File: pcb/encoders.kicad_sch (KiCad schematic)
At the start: 10 parts, among them J1 GPIO, J2 Screw_Terminal_01x04, J3 Screw_Terminal_01x04, J4 Screw_Terminal_01x04

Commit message: update PCB to add two more terminals
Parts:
- added J5, J6: Screw_Terminal_01x04, TerminalBlock_Phoenix:TerminalBlock_Phoenix_PT-1,5-4-5.0-H_1x04_P5.00mm_Horizontal, symbol Connector:Screw_Terminal_01x04
- added R10, R7, R8, R9: 4.7K, Resistor_THT:R_Axial_DIN0207_L6.3mm_D2.5mm_P7.62mm_Horizontal, symbol Device:R
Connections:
- net +3V3: now also R10.1, R7.1, R8.1, R9.1; no longer J1.17 (Pin_17)
- net +5V: now also J5.4 (Pin_4), J6.4 (Pin_4)
- net GND: now also J5.1 (Pin_1), J6.1 (Pin_1)
- net GPIO10/SPI0.MOSI: now also J5.3 (Pin_3), R7.2
- net GPIO11/SPI0.SCLK: now also J6.3 (Pin_3), R9.2
- net GPIO17: now also R4.2; no longer R3.2
- net GPIO22: now also J4.2 (Pin_2), R6.2
- net GPIO27: now also J4.3 (Pin_3), R5.2; no longer J3.3 (Pin_3), R4.2
- net GPIO2/SDA1: now also J2.3 (Pin_3); no longer J2.2 (Pin_2)
- net GPIO3/SCL1: now also J2.2 (Pin_2); no longer J2.3 (Pin_3)
- net GPIO4/GPCLK0: now also J3.3 (Pin_3), R3.2
- net GPIO5: now also J6.2 (Pin_2), R10.2; no longer J4.2 (Pin_2), R5.2
- net GPIO6: no longer J4.3 (Pin_3), R6.2
- net GPIO9/SPI0.MISO: now also J5.2 (Pin_2), R8.2
- no-connect marks 22 -> 19
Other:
- moved on the sheet: J1, J2, J3, J4, R1, R2, R3, R4, R5, R6

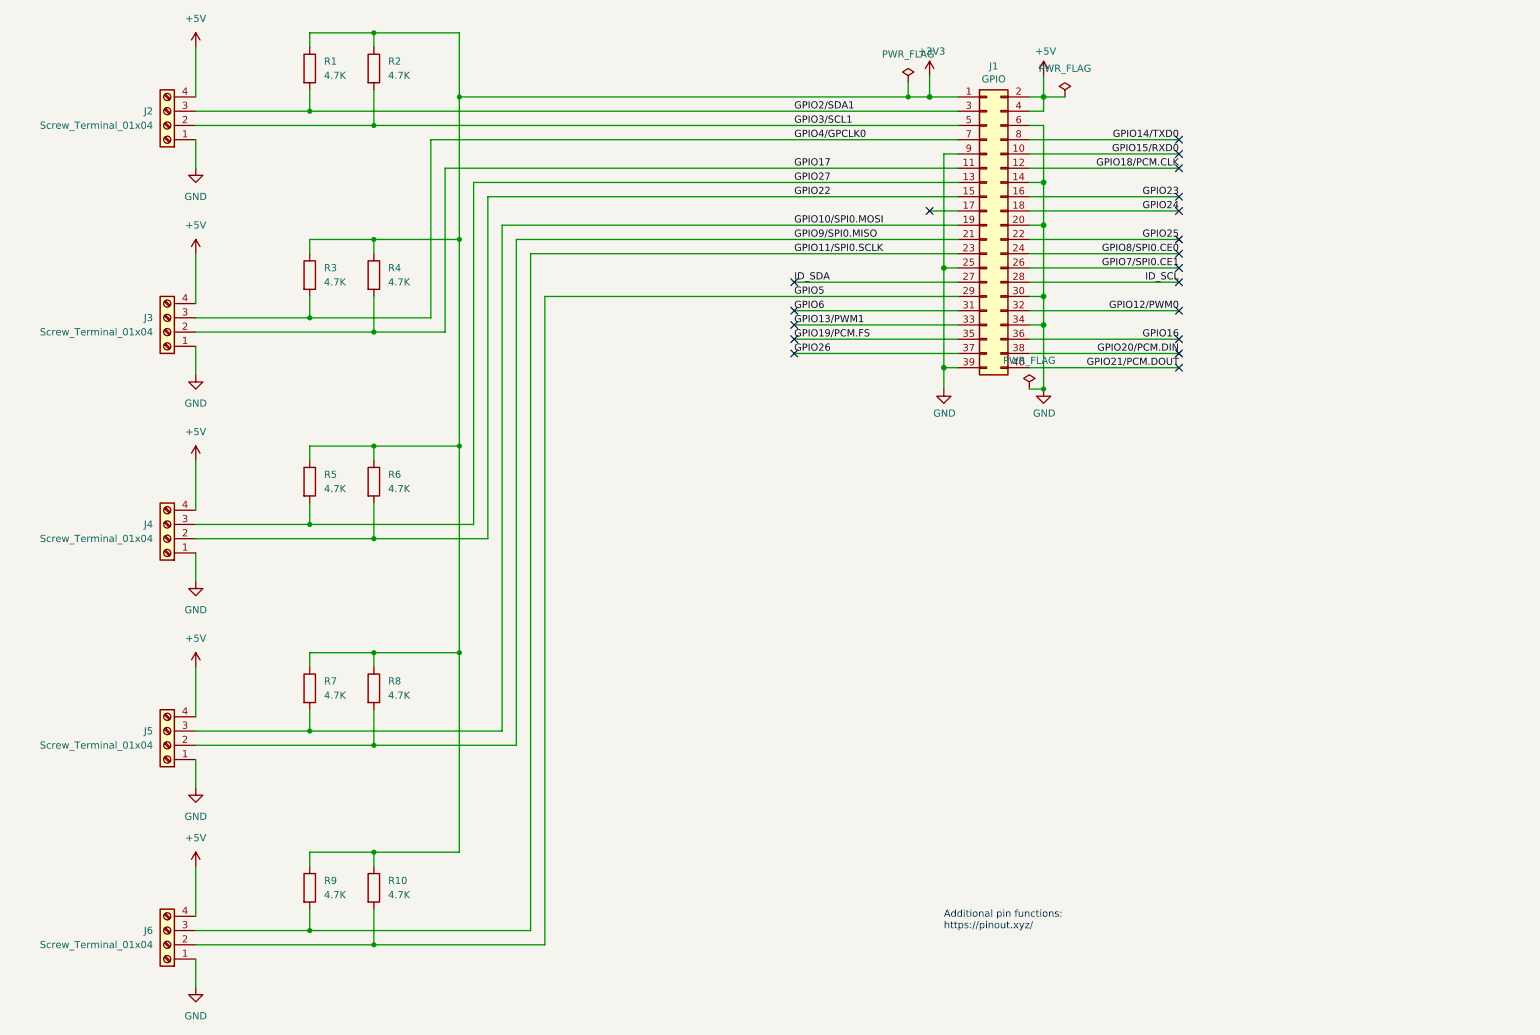
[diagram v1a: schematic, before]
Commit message: updated schematic using ls7466s
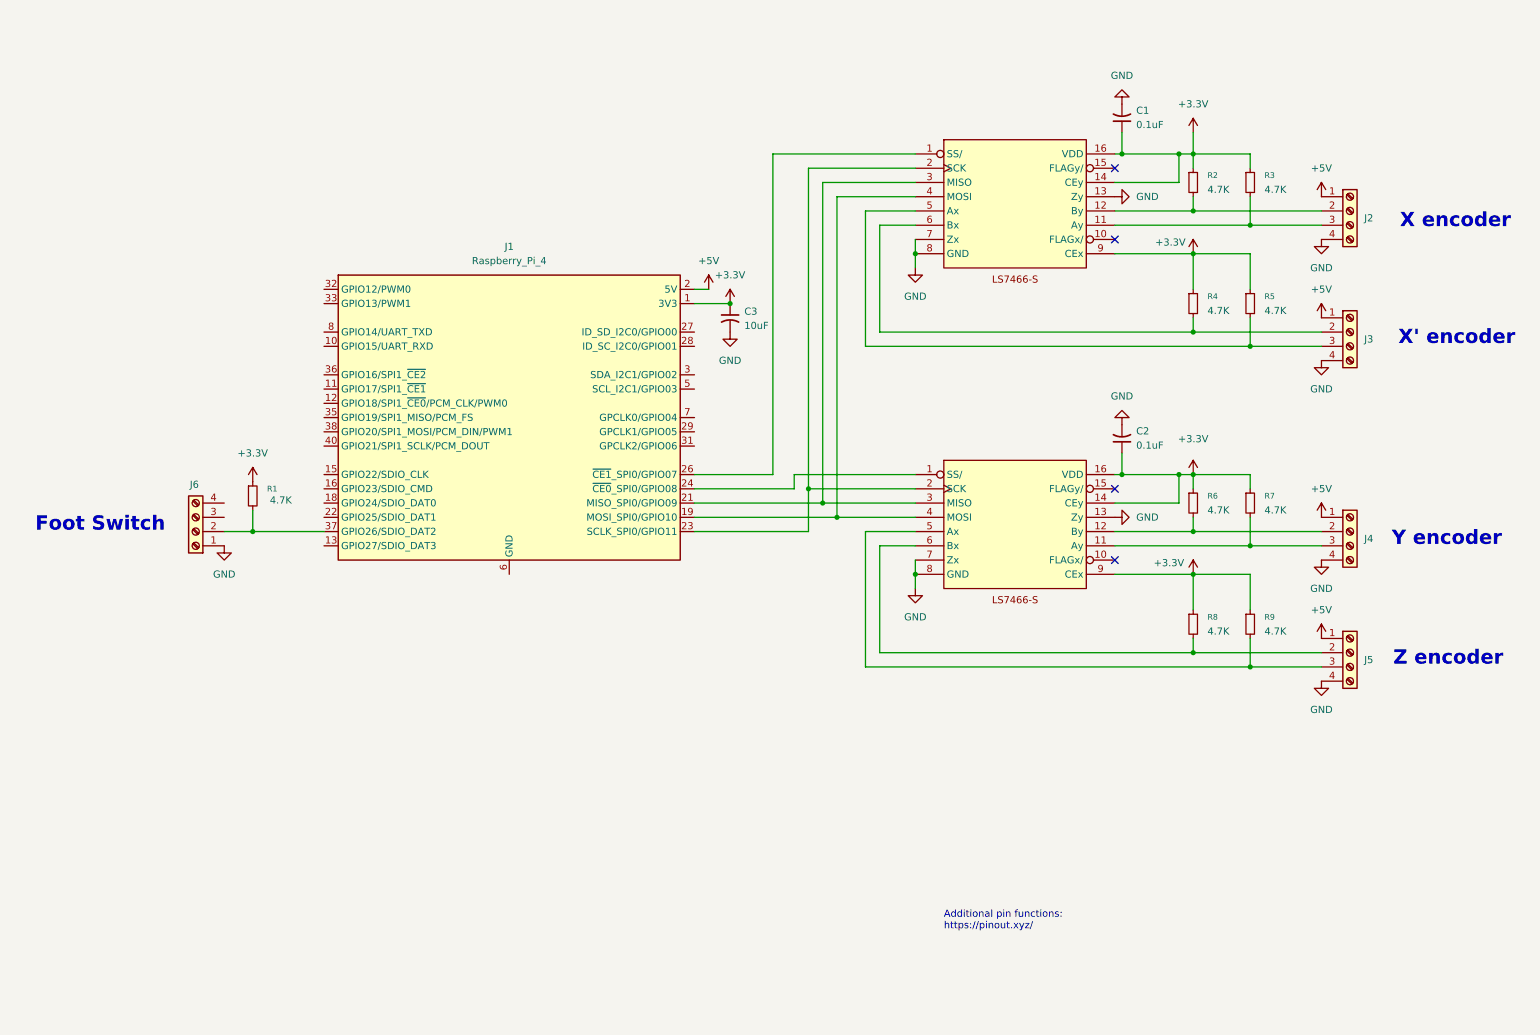
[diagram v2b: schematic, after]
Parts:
- removed J1: GPIO, Connector_PinSocket_2.54mm:PinSocket_2x20_P2.54mm_Vertical, symbol Connector_Generic:Conn_02x20_Odd_Even
- removed R1, R10, R2, R3, R4, R5, R6, R7, R8, R9: 4.7K, Resistor_THT:R_Axial_DIN0207_L6.3mm_D2.5mm_P7.62mm_Horizontal, symbol Device:R
- added C1, C2: 0.1uF, symbol Device:C_Small_US
- added C3: 10uF, symbol Device:C_Small_US
- added J1: Raspberry_Pi_4, symbol Connector:Raspberry_Pi_4
- added LS7466-S1, LS7466-S2: ~, Package_SO:SOIC-16_3.9x9.9mm_P1.27mm, symbol LS7466:LS7466-S
- added R1, R3, R4, R5, R6, R7, R8, R9: 4.7K, symbol Device:R_Small
- added R2: 4.7K, Resistor_SMD:R_0201_0603Metric, symbol Device:R_Small
- J2, J3, J4, J5, J6: footprint TerminalBlock_Phoenix:TerminalBlock_Phoenix_PT-1,5-4-5.0-H_1x04_P5.00mm_Horizontal -> (none)
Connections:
- net +5V: now also J2.1 (Pin_1), J3.1 (Pin_1), J4.1 (Pin_1), J5.1 (Pin_1), J1.2 (5V), J1.4 (5V); no longer J2.4 (Pin_4), J3.4 (Pin_4), J4.4 (Pin_4), J5.4 (Pin_4), J6.4 (Pin_4)
- net GND: now also J2.4 (Pin_4), J3.4 (Pin_4), J4.4 (Pin_4), J5.4 (Pin_4), C1.2, C2.2, C3.2, LS7466-S1.13 (Zy), LS7466-S1.7 (Zx), LS7466-S1.8 (GND), LS7466-S2.13 (Zy), LS7466-S2.7 (Zx), LS7466-S2.8 (GND); no longer J2.1 (Pin_1), J3.1 (Pin_1), J4.1 (Pin_1), J5.1 (Pin_1)
- net GPIO10/SPI0.MOSI: no longer names the net of J5.3 (Pin_3)
- net GPIO10/SPI0.MOSI: now also LS7466-S2.5 (Ax), R9.2
- net GPIO11/SPI0.SCLK: no longer names the net of J6.3 (Pin_3)
- net GPIO17: no longer names the net of J3.2 (Pin_2)
- net GPIO17: now also LS7466-S1.6 (Bx), R4.2
- net GPIO22: no longer names the net of J4.2 (Pin_2)
- net GPIO22: now also LS7466-S2.12 (By), R6.2
- net GPIO27: no longer names the net of J4.3 (Pin_3)
- net GPIO27: now also LS7466-S2.11 (Ay), R7.2
- net GPIO2/SDA1: no longer names the net of J2.3 (Pin_3)
- net GPIO2/SDA1: now also LS7466-S1.11 (Ay), R3.2
- net GPIO3/SCL1: no longer names the net of J2.2 (Pin_2)
- net GPIO3/SCL1: now also LS7466-S1.12 (By), R2.2
- net GPIO4/GPCLK0: no longer names the net of J3.3 (Pin_3)
- net GPIO4/GPCLK0: now also LS7466-S1.5 (Ax), R5.2
- net GPIO5: no longer names the net of J6.2 (Pin_2)
- net GPIO5: now also J1.37 (GPIO26/SDIO_DAT2), R1.2
- net GPIO9/SPI0.MISO: no longer names the net of J5.2 (Pin_2)
- net GPIO9/SPI0.MISO: now also LS7466-S2.6 (Bx), R8.2
- new net: J1.26 (~{CE1}_SPI0/GPIO07), LS7466-S1.1 (SS/)
- new net: J1.23 (SCLK_SPI0/GPIO11), LS7466-S1.2 (SCK), LS7466-S2.2 (SCK)
- new net: J1.21 (MISO_SPI0/GPIO09), LS7466-S1.3 (MISO), LS7466-S2.3 (MISO)
- new net: J1.19 (MOSI_SPI0/GPIO10), LS7466-S1.4 (MOSI), LS7466-S2.4 (MOSI)
- new net: J1.14 (GND), J1.20 (GND), J1.25 (GND), J1.30 (GND), J1.34 (GND), J1.39 (GND), J1.6 (GND), J1.9 (GND)
- new net: J1.24 (~{CE0}_SPI0/GPIO08), LS7466-S2.1 (SS/)
- new net +3.3V: C1.1, C2.1, C3.1, J1.1 (3V3), J1.17 (3V3), LS7466-S1.14 (CEy), LS7466-S1.16 (VDD), LS7466-S1.9 (CEx), LS7466-S2.14 (CEy), LS7466-S2.16 (VDD), LS7466-S2.9 (CEx), R1.1, R2.1, R3.1, R4.1, R5.1, R6.1, R7.1, R8.1, R9.1
- no-connect marks 19 -> 4
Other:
- note added: "Foot Switch"
- note added: "X encoder"
- note added: "X' encoder"
- note added: "Y encoder"
- note added: "Z encoder"

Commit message: add footprints
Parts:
- C1, C2: footprint (none) -> Capacitor_SMD:C_0603_1608Metric
- C3: footprint (none) -> Capacitor_SMD:C_0805_2012Metric
- J1: footprint (none) -> Connector_PinSocket_2.54mm:PinSocket_2x20_P2.54mm_Vertical
- J2, J3, J4, J5, J6: footprint (none) -> TerminalBlock_Phoenix:TerminalBlock_Phoenix_PT-1,5-4-5.0-H_1x04_P5.00mm_Horizontal
- R1, R3, R4, R5, R6, R7, R8, R9: footprint (none) -> Resistor_SMD:R_0603_1608Metric
- R2: footprint Resistor_SMD:R_0201_0603Metric -> Resistor_SMD:R_0603_1608Metric
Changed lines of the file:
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@@
 			)
 		)
-		(property "Footprint" ""
+		(property "Footprint" "TerminalBlock_Phoenix:TerminalBlock_Phoenix_PT-1,5-4-5.0-H_1x04_P5.00mm_Horizontal"
 			(at 251.46 109.22 0)
 			(effects
@@
 			)
 		)
-		(property "Footprint" ""
+		(property "Footprint" "Resistor_SMD:R_0603_1608Metric"
 			(at 233.68 46.99 0)
 			(effects
@@
 			)
 		)
-		(property "Footprint" ""
+		(property "Footprint" "TerminalBlock_Phoenix:TerminalBlock_Phoenix_PT-1,5-4-5.0-H_1x04_P5.00mm_Horizontal"
 			(at 251.46 130.81 0)
 			(effects
@@
 			)
 		)
-		(property "Footprint" ""
+		(property "Footprint" "Resistor_SMD:R_0603_1608Metric"
 			(at 233.68 68.58 0)
 			(effects
@@
 			)
 		)
-		(property "Footprint" ""
+		(property "Footprint" "TerminalBlock_Phoenix:TerminalBlock_Phoenix_PT-1,5-4-5.0-H_1x04_P5.00mm_Horizontal"
 			(at 45.72 109.22 0)
 			(effects
@@
 			)
 		)
-		(property "Footprint" ""
+		(property "Footprint" "Resistor_SMD:R_0603_1608Metric"
 			(at 55.88 102.87 0)
 			(effects
@@
 			)
 		)
-		(property "Footprint" "Resistor_SMD:R_0201_0603Metric"
+		(property "Footprint" "Resistor_SMD:R_0603_1608Metric"
 			(at 223.52 46.99 0)
 			(effects
@@
 			)
 		)
-		(property "Footprint" ""
+		(property "Footprint" "Resistor_SMD:R_0603_1608Metric"
 			(at 223.52 125.73 0)
 			(effects
@@
 			)
 		)
-		(property "Footprint" ""
+		(property "Footprint" "Resistor_SMD:R_0603_1608Metric"
 			(at 223.52 104.14 0)
 			(effects
@@
 			)
 		)
-		(property "Footprint" ""
+		(property "Footprint" "Capacitor_SMD:C_0603_1608Metric"
 			(at 210.82 92.71 0)
 			(effects
@@
 			)
 		)
-		(property "Footprint" ""
+		(property "Footprint" "Capacitor_SMD:C_0805_2012Metric"
 			(at 140.97 71.12 0)
 			(effects
@@
 			)
 		)
-		(property "Footprint" ""
+		(property "Footprint" "TerminalBlock_Phoenix:TerminalBlock_Phoenix_PT-1,5-4-5.0-H_1x04_P5.00mm_Horizontal"
 			(at 251.46 73.66 0)
 			(effects
@@
 			)
 		)
-		(property "Footprint" ""
+		(property "Footprint" "Resistor_SMD:R_0603_1608Metric"
 			(at 223.52 68.58 0)
 			(effects
@@
 			)
 		)
-		(property "Footprint" ""
+		(property "Footprint" "Resistor_SMD:R_0603_1608Metric"
 			(at 233.68 104.14 0)
 			(effects
@@
 			)
 		)
-		(property "Footprint" ""
+		(property "Footprint" "Resistor_SMD:R_0603_1608Metric"
 			(at 233.68 125.73 0)
 			(effects
@@
 			)
 		)
-		(property "Footprint" ""
+		(property "Footprint" "Capacitor_SMD:C_0603_1608Metric"
 			(at 210.82 35.56 0)
 			(effects
@@
 			)
 		)
-		(property "Footprint" ""
+		(property "Footprint" "TerminalBlock_Phoenix:TerminalBlock_Phoenix_PT-1,5-4-5.0-H_1x04_P5.00mm_Horizontal"
 			(at 251.46 52.07 0)
 			(effects
@@
 			)
 		)
-		(property "Footprint" ""
+		(property "Footprint" "Connector_PinSocket_2.54mm:PinSocket_2x20_P2.54mm_Vertical"
 			(at 171.704 136.398 0)
 			(effects
